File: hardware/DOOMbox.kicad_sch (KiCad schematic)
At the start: 36 parts, among them J1 DE15_Socket_HighDensity, J2 AudioJack3, SW1 SW_SPST, SW2 SW_Push, U1 RPi Pico 2, U2 AP7381-50SA-7, U3 LM324N, U4 CD4010BE

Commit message: Shorten R12 and R13 + add missing cut
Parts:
- R12: footprint Resistor_THT:R_Axial_DIN0309_L9.0mm_D3.2mm_P12.70mm_Horizontal -> Resistor_THT:R_Axial_DIN0207_L6.3mm_D2.5mm_P10.16mm_Horizontal
- R13: footprint Resistor_THT:R_Axial_DIN0309_L9.0mm_D3.2mm_P12.70mm_Horizontal -> Resistor_THT:R_Axial_DIN0207_L6.3mm_D2.5mm_P7.62mm_Horizontal
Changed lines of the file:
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@@
 			)
 		)
-		(property "Footprint" "Resistor_THT:R_Axial_DIN0309_L9.0mm_D3.2mm_P12.70mm_Horizontal"
+		(property "Footprint" "Resistor_THT:R_Axial_DIN0207_L6.3mm_D2.5mm_P10.16mm_Horizontal"
 			(at 160.02 46.228 90)
 			(effects
@@
 			)
 		)
-		(property "Footprint" "Resistor_THT:R_Axial_DIN0309_L9.0mm_D3.2mm_P12.70mm_Horizontal"
+		(property "Footprint" "Resistor_THT:R_Axial_DIN0207_L6.3mm_D2.5mm_P7.62mm_Horizontal"
 			(at 160.02 72.898 90)
 			(effects

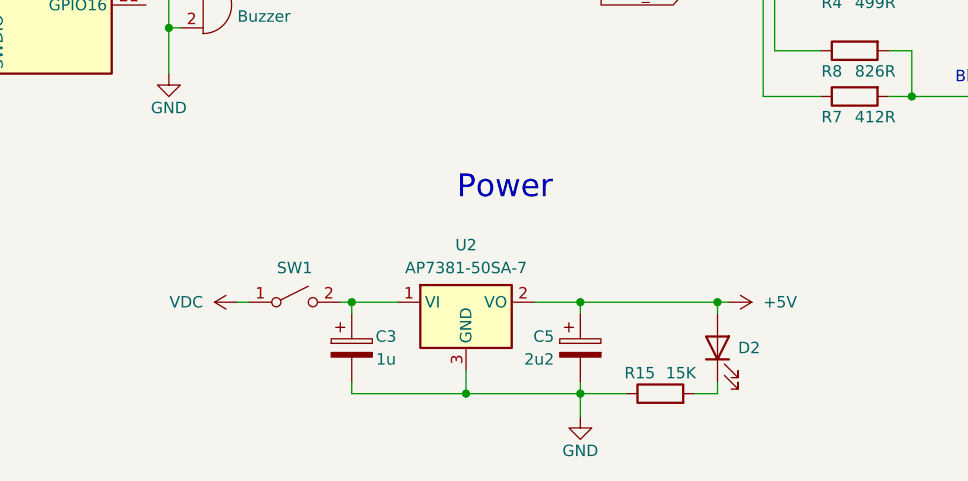
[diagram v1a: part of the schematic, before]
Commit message: Fix incorrect pins on U2 and accidental stripboard cut in U4
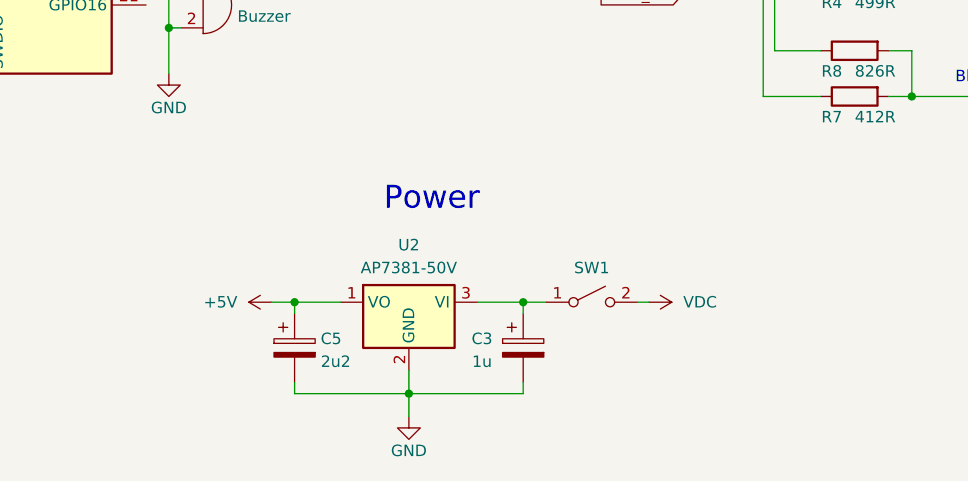
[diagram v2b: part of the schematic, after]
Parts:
- removed D2: LED, Stripboard:Peripheral_Offboard, symbol Device:LED
- removed R15: 15K, Resistor_THT:R_Axial_DIN0309_L9.0mm_D3.2mm_P5.08mm_Vertical, symbol Device:R
- removed U2: AP7381-50SA-7, Package_TO_SOT_THT:TO-92_Inline_Wide, symbol Regulator_Linear:AP7381-50SA-7
- added U2: AP7381-50V, AP7381:AP7381-TO92, symbol AP7381:AP7381-50V-TO92
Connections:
- net +5V: now also U2.1 (VO)
- net GND: now also U2.2 (GND)
- net VDC: now also SW1.2 (B); no longer SW1.1 (A)
- net at C3.1: now also SW1.1 (A), U2.3 (VI); no longer SW1.2 (B)
